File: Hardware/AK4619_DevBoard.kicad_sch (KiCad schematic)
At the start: 41 parts, among them J1 Out, J10 Conn_02x17_Odd_Even, J2 In, J7 Conn_02x10_Odd_Even, J8 Conn_02x08_Odd_Even, J9 Conn_02x15_Odd_Even, U2 AK4619VN

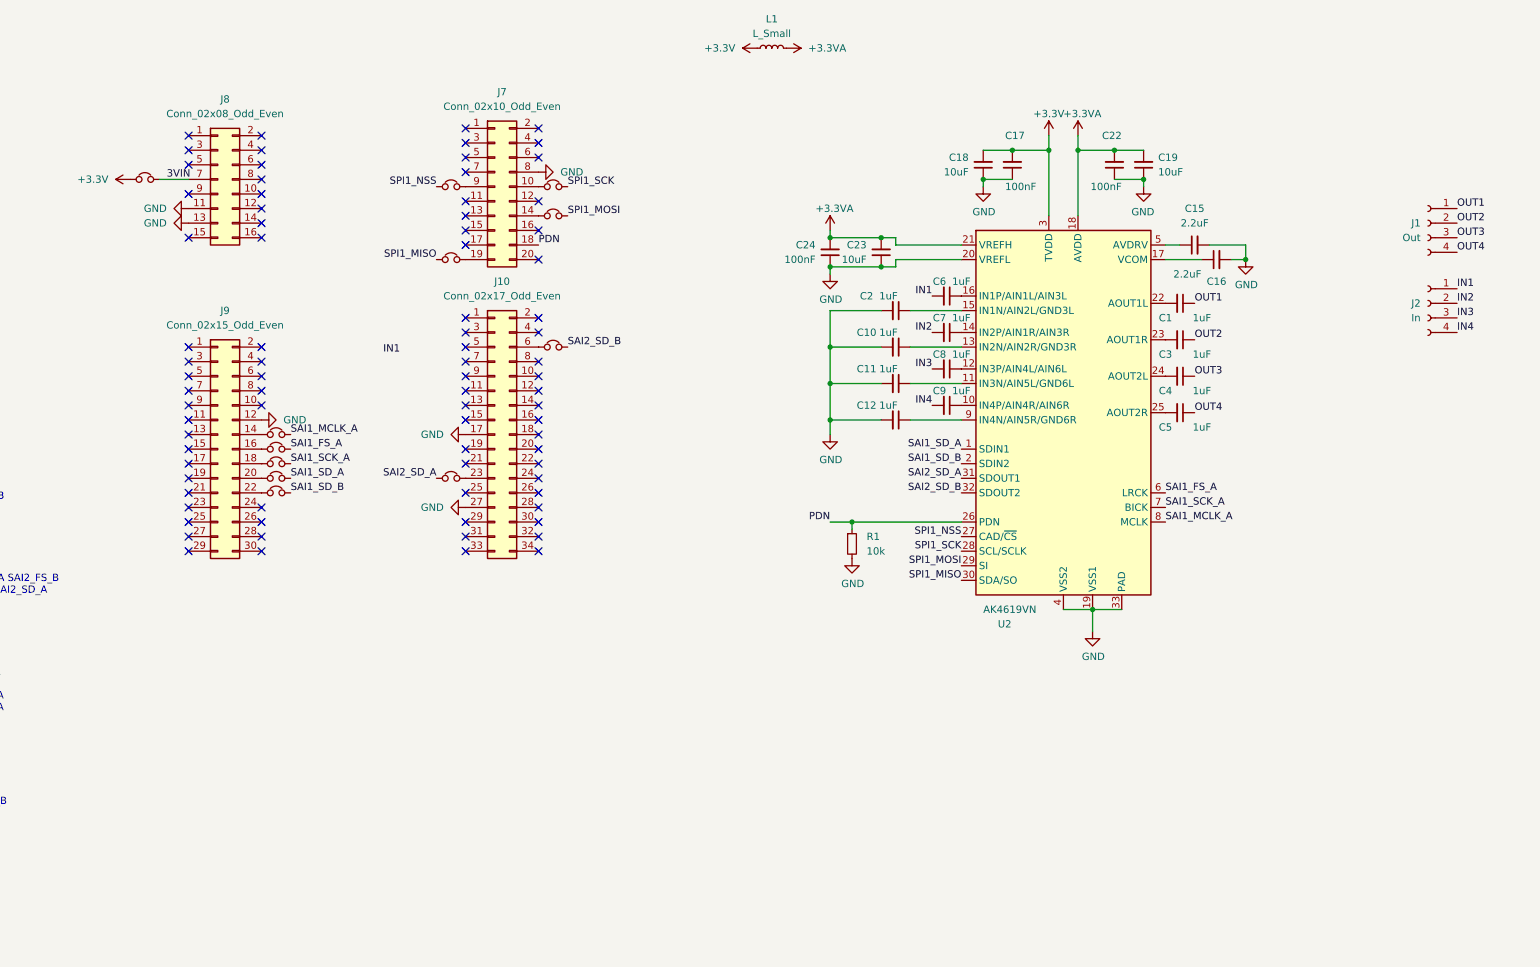
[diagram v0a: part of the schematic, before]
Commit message: Added HyperRam to Dev Board
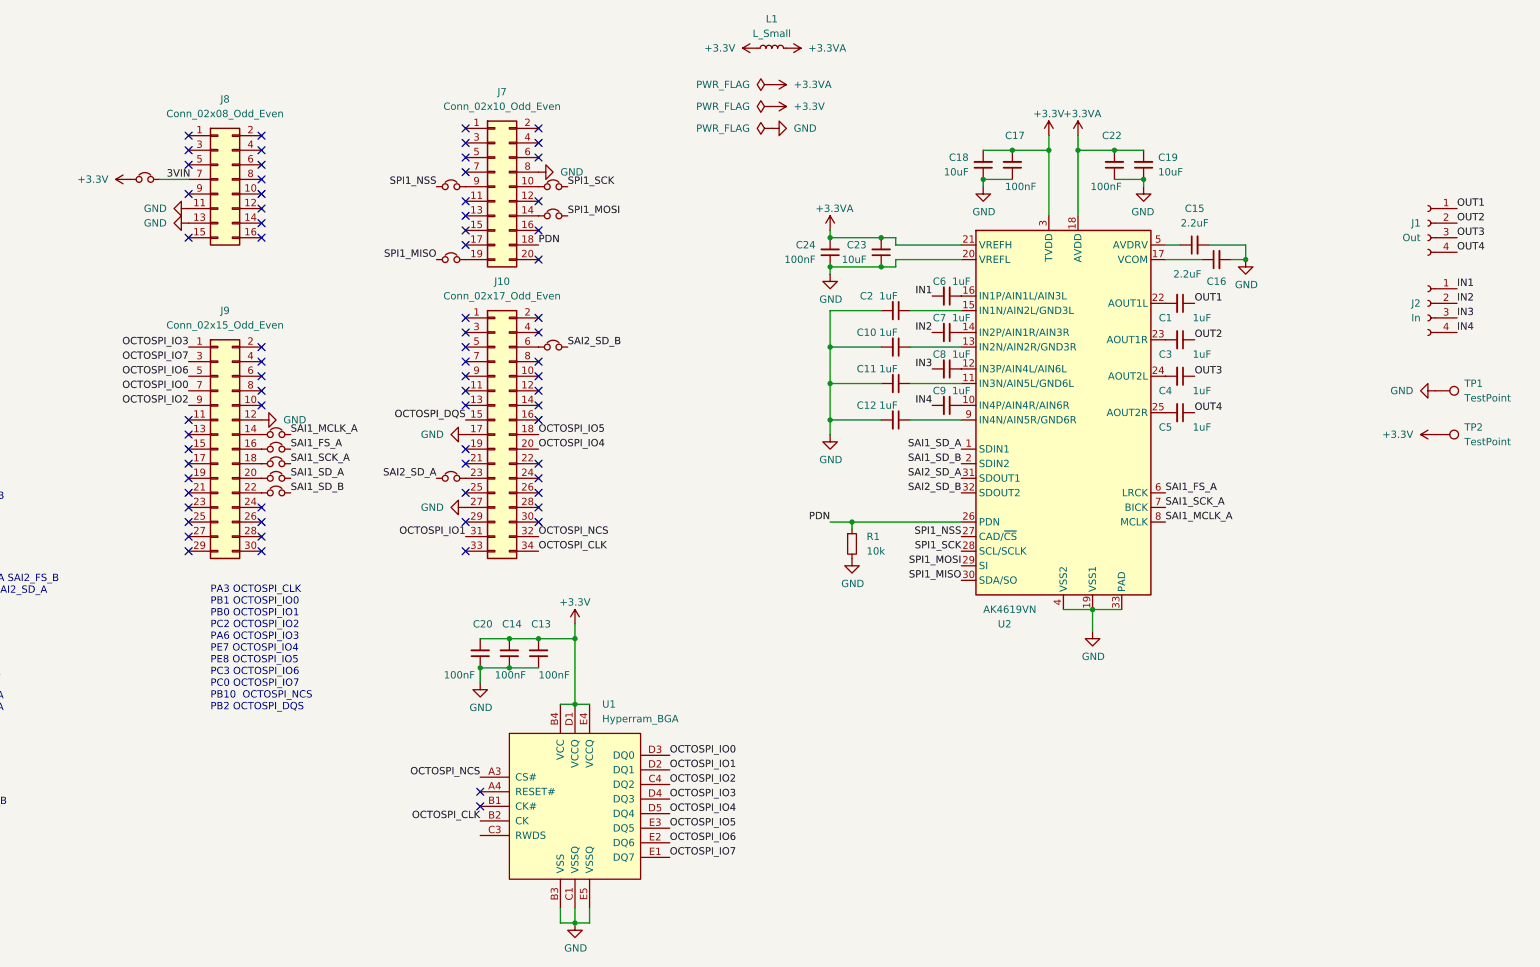
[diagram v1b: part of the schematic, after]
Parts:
- added C13, C14, C20: 100nF, Capacitor_SMD:C_0603_1608Metric_Pad1.08x0.95mm_HandSolder, symbol Device:C_Small
- added TP1, TP2: TestPoint, Custom_Footprints:1mm_Test_Point, symbol Connector:TestPoint
- added U1: Hyperram_BGA, Custom_Footprints:BGA-24_5x5_6.0x8.0mm, symbol Hyperram:Hyperram_BGA
- U2: footprint Package_DFN_QFN:QFN-32-1EP_5x5mm_P0.5mm_EP3.1x3.1mm_ThermalVias -> Custom_Footprints:QFN-32-1EP_5x5mm_P0.5mm_EP3.1x3.1mm_ThermalVias
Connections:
- net GND: now also C13.1, C14.1, C20.1, TP1.1, U1.B3 (VSS), U1.C1 (VSSQ), U1.E5 (VSSQ)
- net OCTOSPI_DQS: now reaches J10.15 (Pin_15)
- net OCTOSPI_IO5: now reaches J10.18 (Pin_18)
- net OCTOSPI_IO5: now also U1.E3 (DQ5)
- net OCTOSPI_IO4: now reaches J10.20 (Pin_20)
- net OCTOSPI_IO4: now also U1.D5 (DQ4)
- net OCTOSPI_IO1: now reaches J10.31 (Pin_31)
- net OCTOSPI_IO1: now also U1.D2 (DQ1)
- net OCTOSPI_NCS: now reaches J10.32 (Pin_32)
- net OCTOSPI_NCS: now also U1.A3 (CS#)
- net OCTOSPI_CLK: now reaches J10.34 (Pin_34)
- net OCTOSPI_CLK: now also U1.B2 (CK)
- net OCTOSPI_IO3: now reaches J9.1 (Pin_1)
- net OCTOSPI_IO3: now also U1.D4 (DQ3)
- net OCTOSPI_IO7: now reaches J9.3 (Pin_3)
- net OCTOSPI_IO7: now also U1.E1 (DQ7)
- net OCTOSPI_IO6: now reaches J9.5 (Pin_5)
- net OCTOSPI_IO6: now also U1.E2 (DQ6)
- net OCTOSPI_IO0: now reaches J9.7 (Pin_7)
- net OCTOSPI_IO0: now also U1.D3 (DQ0)
- net OCTOSPI_IO2: now reaches J9.9 (Pin_9)
- net OCTOSPI_IO2: now also U1.C4 (DQ2)
- net +3V3 renamed +3.3V
- net +3.3V: now also C13.2, C14.2, C20.2, TP2.1, U1.B4 (VCC), U1.D1 (VCCQ), U1.E4 (VCCQ)
- new net: U1.A2 (RFU), U1.A5 (RFU), U1.B5 (RFU), U1.C2 (RFU), U1.C5 (RFU)
- no-connect marks 81 -> 72
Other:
- note added: "PA3 OCTOSPI_CLK PB1 OCTOSPI_IO0 PB0 OCTOSPI_IO1 PC2 OCTOSPI_IO2 PA6 OCTOSPI_IO3 PE7 OCTOSPI_IO4 PE8 OCTOSPI_IO5 PC3 OCTOSPI_IO6 PC0 OCTOSPI_IO7 PB10 OCTOSPI_NCS PB2 OCTOSPI_DQS"

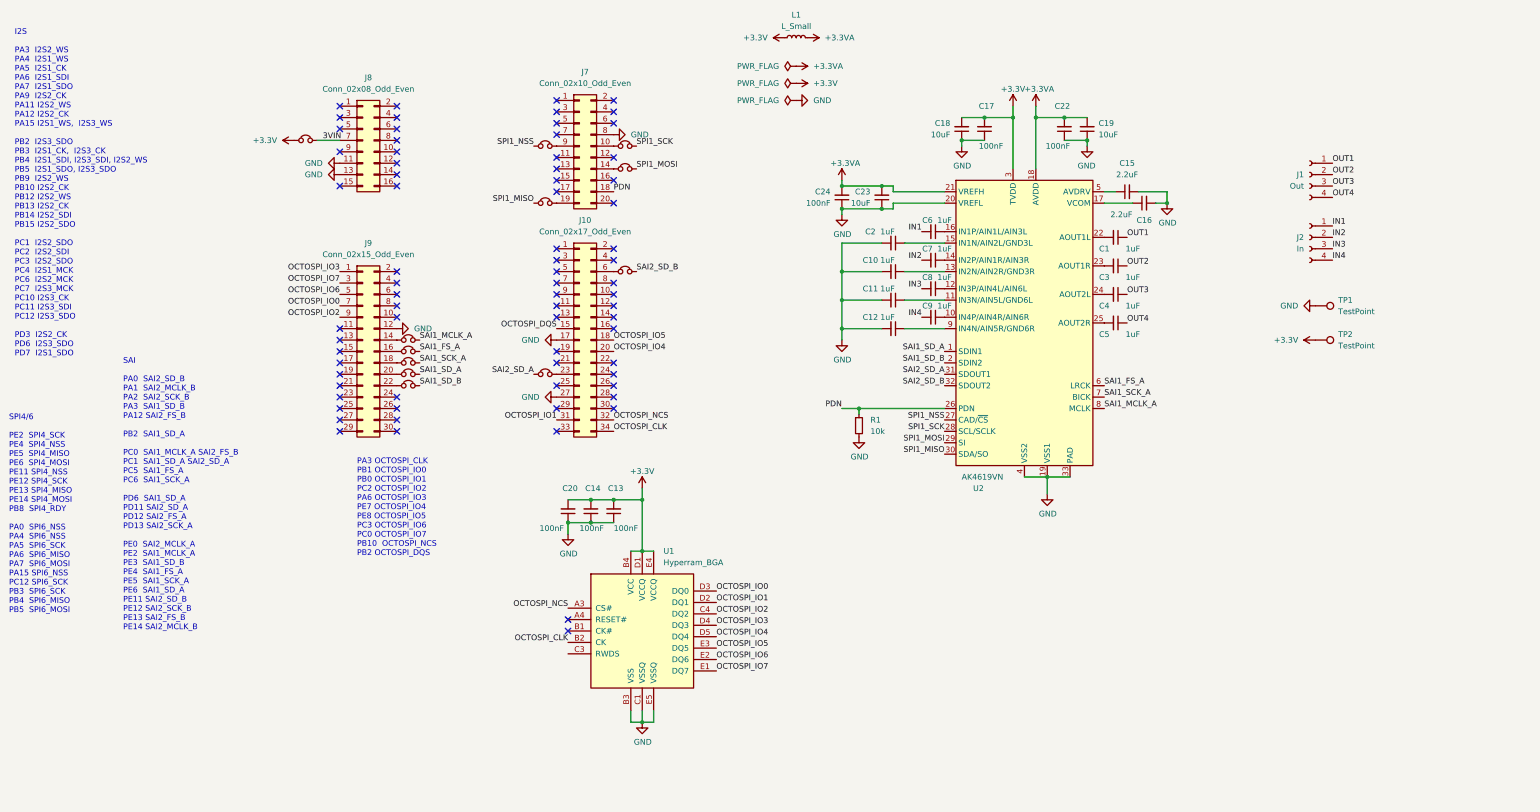
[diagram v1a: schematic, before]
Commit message: Added Input scaling
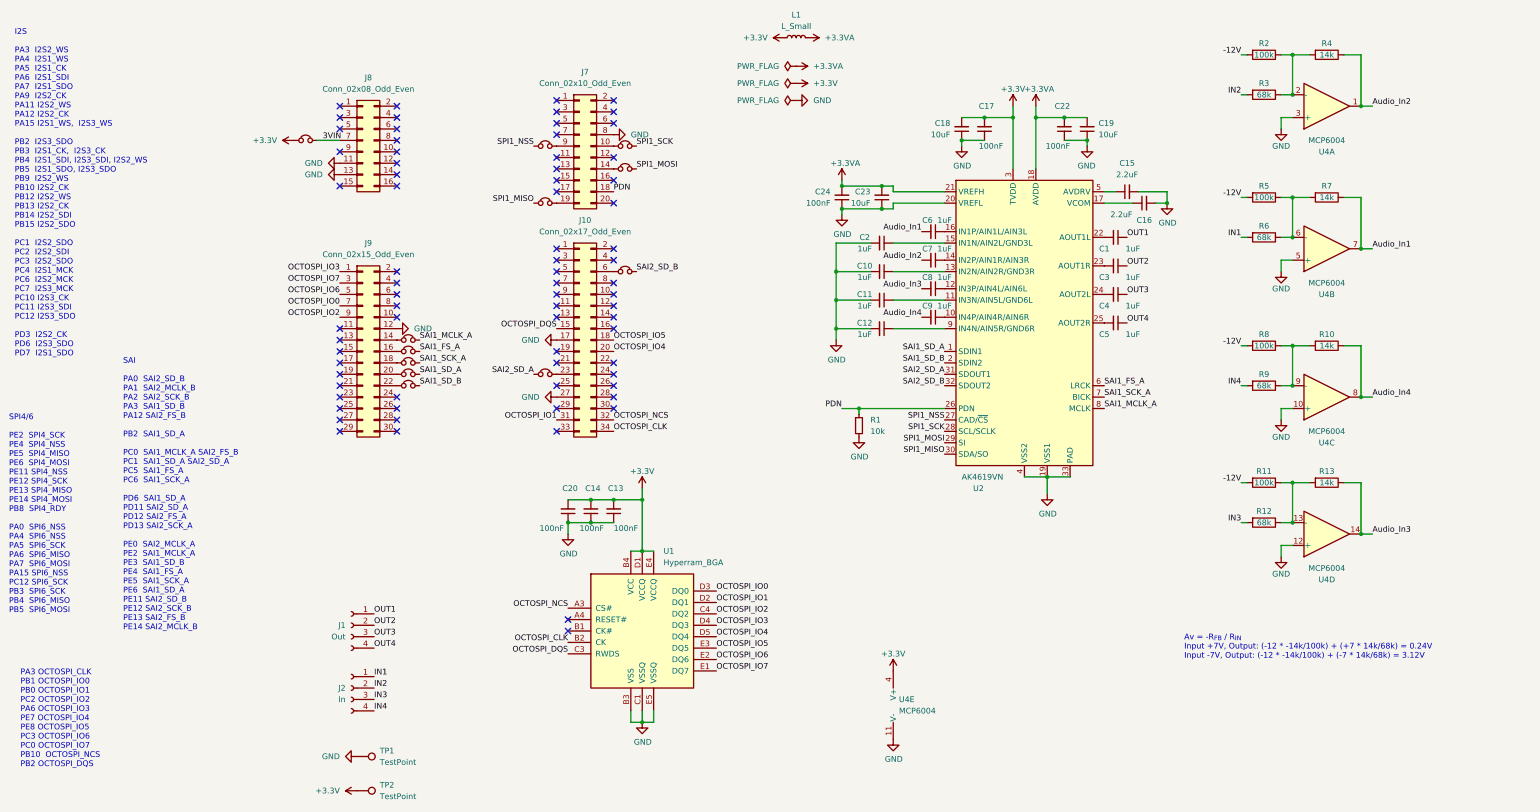
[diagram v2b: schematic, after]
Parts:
- added R10, R13, R4, R7: 14k, Resistor_SMD:R_0603_1608Metric_Pad0.98x0.95mm_HandSolder, symbol Device:R
- added R11, R2, R5, R8: 100k, Resistor_SMD:R_0603_1608Metric_Pad0.98x0.95mm_HandSolder, symbol Device:R
- added R12, R3, R6, R9: 68k, Resistor_SMD:R_0603_1608Metric_Pad0.98x0.95mm_HandSolder, symbol Device:R
- added U4: MCP6004, Package_SO:SO-14_3.9x8.65mm_P1.27mm, symbol Amplifier_Operational:MCP6004
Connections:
- net +3.3V: now also U4.4 (V+)
- net GND: now also U4.10 (+), U4.11 (V-), U4.12 (+), U4.3 (+), U4.5 (+)
- net IN1: now also R6.2; no longer C6.2
- net IN2: now also R3.2; no longer C7.2
- net IN3: now also R12.2; no longer C8.2
- net IN4: now also R9.2; no longer C9.2
- net OCTOSPI_DQS: now also U1.C3 (RWDS)
- new net: R2.1, R3.1, R4.2, U4.2 (-)
- new net: R10.2, R8.1, R9.1, U4.9 (-)
- new net: R5.1, R6.1, R7.2, U4.6 (-)
- new net: R11.1, R12.1, R13.2, U4.13 (-)
- new net -12V: R11.2, R2.2, R5.2, R8.2
- new net Audio_In1: C6.2, R7.1, U4.7
- new net Audio_In2: C7.2, R4.1, U4.1
- new net Audio_In3: C8.2, R13.1, U4.14
- new net Audio_In4: C9.2, R10.1, U4.8
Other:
- note added: "Av = -R_{FB} / R_{IN} Input +7V, Output: (-12 * -14k/100k) + (+7 * 14k/68k) = 0.24V Input -7V, Output: (-12 * -14k/100k) + (-7 * 14k/68k) = 3.12V"
- moved on the sheet: C10, C11, C12, C2, J1, J2, TP1, TP2

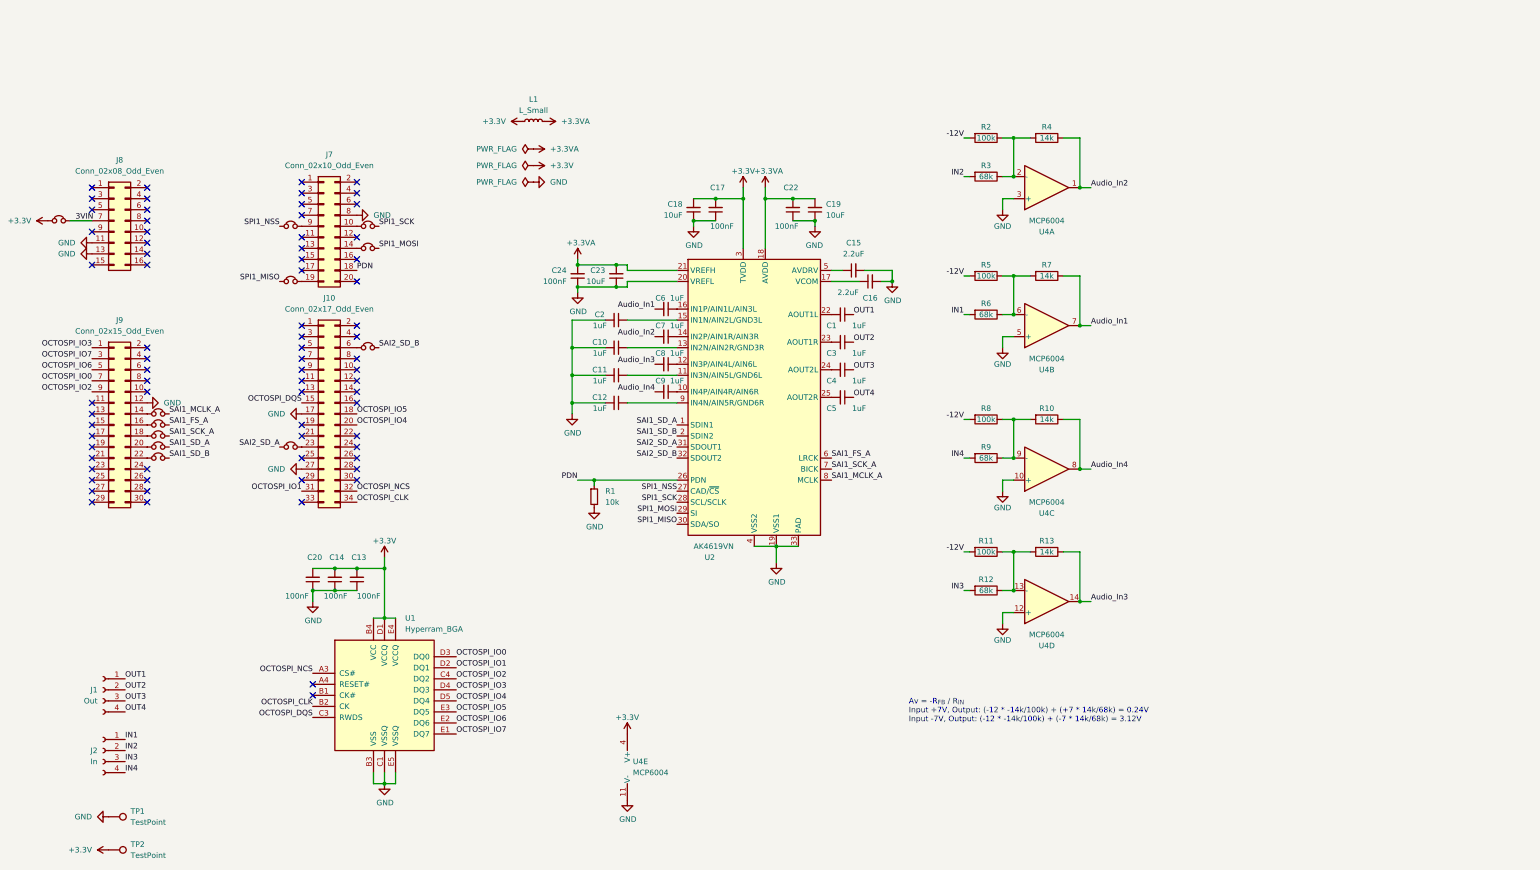
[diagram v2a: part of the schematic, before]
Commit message: Added Ouput op-amp
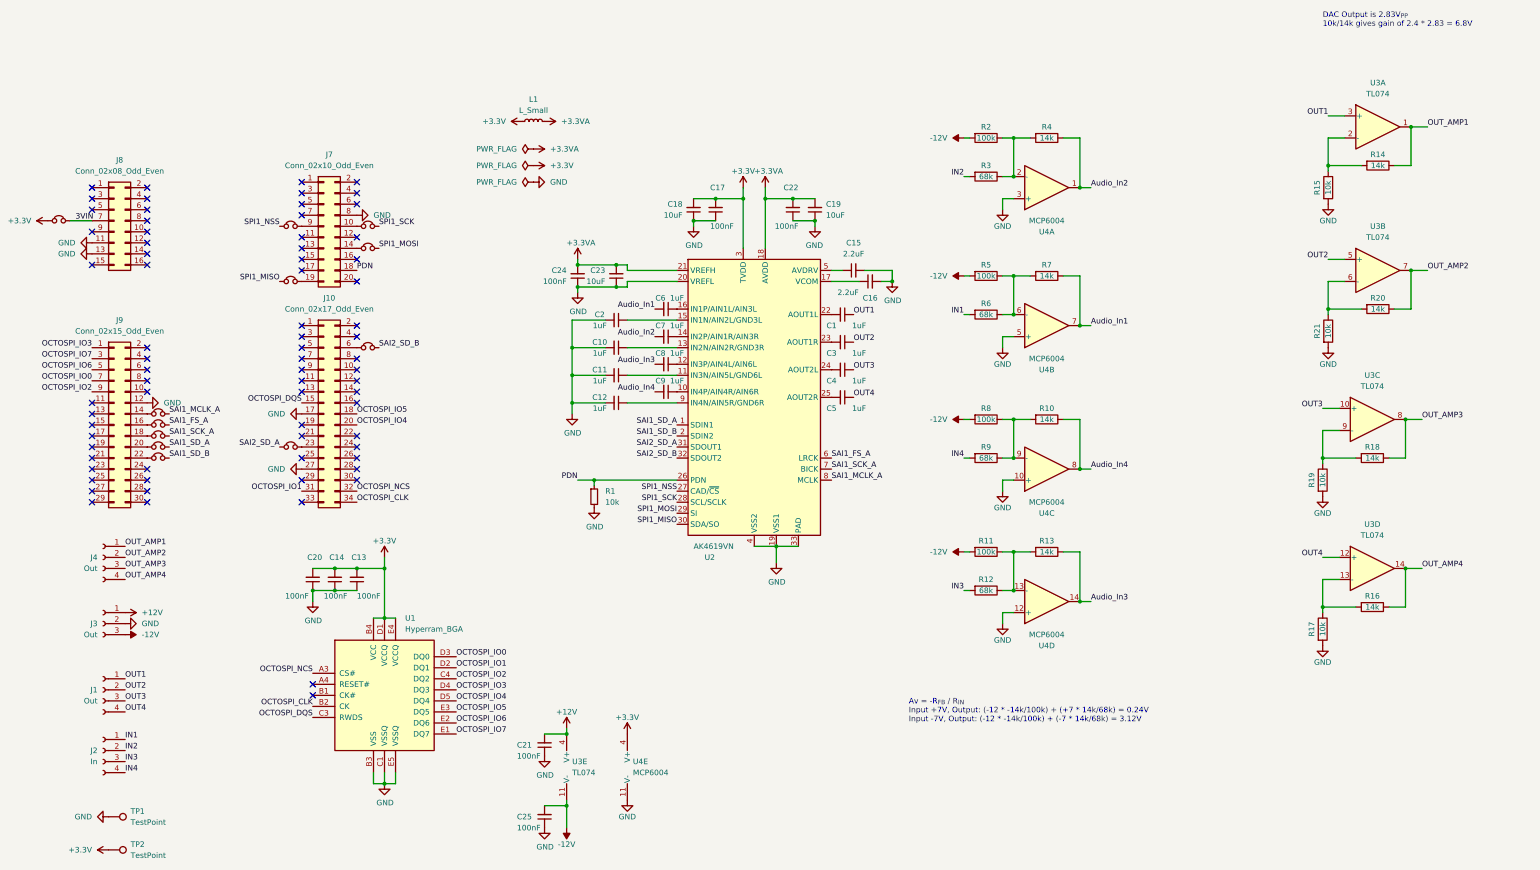
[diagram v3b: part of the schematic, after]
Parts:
- added C21, C25: 100nF, Capacitor_SMD:C_0603_1608Metric_Pad1.08x0.95mm_HandSolder, symbol Device:C_Small
- added J3: Out, Connector_PinSocket_2.54mm:PinSocket_1x03_P2.54mm_Vertical, symbol Connector:Conn_01x03_Socket
- added J4: Out, Connector_PinSocket_2.54mm:PinSocket_1x04_P2.54mm_Vertical, symbol Connector:Conn_01x04_Socket
- added R14, R16, R18, R20: 14k, Resistor_SMD:R_0603_1608Metric_Pad0.98x0.95mm_HandSolder, symbol Device:R
- added R15, R17, R19, R21: 10k, Resistor_SMD:R_0603_1608Metric_Pad0.98x0.95mm_HandSolder, symbol Device:R
- added U3: TL074, Package_SO:SO-14_3.9x8.65mm_P1.27mm, symbol Amplifier_Operational:TL074
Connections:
- net -12V: now also C25.2, J3.3 (Pin_3), U3.11 (V-)
- net GND: now also C21.1, C25.1, J3.2 (Pin_2), R15.2, R17.2, R19.2, R21.2
- net OUT1: now also U3.3 (+)
- net OUT2: now also U3.5 (+)
- net OUT3: now also U3.10 (+)
- net OUT4: now also U3.12 (+)
- new net: R18.2, R19.1, U3.9 (-)
- new net: R20.2, R21.1, U3.6 (-)
- new net: R16.2, R17.1, U3.13 (-)
- new net: R14.2, R15.1, U3.2 (-)
- new net +12V: C21.2, J3.1 (Pin_1), U3.4 (V+)
- new net OUT_AMP1: J4.1 (Pin_1), R14.1, U3.1
- new net OUT_AMP2: J4.2 (Pin_2), R20.1, U3.7
- new net OUT_AMP3: J4.3 (Pin_3), R18.1, U3.8
- new net OUT_AMP4: J4.4 (Pin_4), R16.1, U3.14
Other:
- note added: "DAC Output is 2.83V_{PP} 10k/14k gives gain of 2.4 * 2.83 = 6.8V"

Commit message: DevBoard Gerbers ordered
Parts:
- added J2: Power, Connector_PinSocket_2.54mm:PinSocket_1x02_P2.54mm_Vertical, symbol Connector:Conn_01x02_Socket
- J1: renamed from J3; value Out -> Power
- J5: renamed from J4; value Out -> Out_Amp
- renumbered C21 to C1, C7 to C10, C8 to C11, C9 to C12, C20 to C13, C18 to C15, C13 to C16, C22 to C18, C25 to C2, C1 to C20, C3 to C21, C4 to C22, C5 to C23, C15 to C24, C16 to C25, C24 to C3, C23 to C4, C2 to C5, C10 to C6, C11 to C7, C12 to C8, C6 to C9, J2 to J3, J1 to J4, J8 to J6, J9 to J7, J7 to J8, J10 to J9, JP12 to JP1, JP3 to JP10, JP1 to JP11, JP5 to JP12, JP11 to JP2, JP10 to JP3, JP9 to JP4, JP8 to JP5, JP7 to JP6, JP2 to JP7, JP4 to JP8, JP6 to JP9, R4 to R10, R7 to R11, R10 to R12, R19 to R14, R17 to R15, R15 to R16, R21 to R17, R16 to R19, R14 to R20, R20 to R21, R5 to R4, R6 to R5, R8 to R6, R9 to R7, R11 to R8, R12 to R9, U3 to U1, U4 to U2, U1 to U3, U2 to U4
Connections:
- net +12V: now also J2.1 (Pin_1)
- net -12V: now also J2.2 (Pin_2)
- net at J8.17 (Pin_17): now also JP7.2
- net at J8.9 (Pin_9): no longer JP7.2
- now unconnected: U3.A2 (RFU), U3.A5 (RFU), U3.B5 (RFU), U3.C2 (RFU), U3.C5 (RFU)
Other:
- note added: "Audio DAC"
- note added: "Av = -R_{FB} / R_{IN} Input: +7V, Output: (-12 * -14k/100k) + (+7 * 14k/68k) = 0.24V Input: -7V Output: (-12 * -14k/100k) + (-7 * 14k/68k) = 3.12V"
- note added: "HyperRAM"
- note added: "I/O and Power"
- note added: "Input/Output OpAmps"
- note added: "Nucleo Connectors"
- note removed: "Av = -R_{FB} / R_{IN} Input +7V, Output: (-12 * -14k/100k) + (+7 * 14k/68k) = 0.24V Input -7V, Output: (-12 * -14k/100k) + (-7 * 14k/68k) = 3.12V"
- company: (none) -> Mountjoy Modular
- title: (none) -> AK4619 STM32H563 Dev Board
- moved on the sheet: C1, C10, C11, C12, C13, C14, C15, C16, C17, C18, C19, C2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
